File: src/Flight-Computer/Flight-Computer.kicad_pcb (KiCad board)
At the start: 4 copper layers, 101.6 x 50.8 mm, 60 parts, among them J1 Jumper_NO, P1 EJ508A, P2 USB, P3 SBH11-PBPC-D05-RA-BK, P4 0901471110, P5 66953-005LF, P6 Micro_SD_Card, P7 0901471110, U1 STM32H750VBTx, U2 LM22672MRE-5.0_NOPB, U3 LMS8117AMP-3.3_NOPB, U4 SN74LV07ADR, U5 SST25VF040B-50-4I-S2AE-T, U6 TPS2115APWR

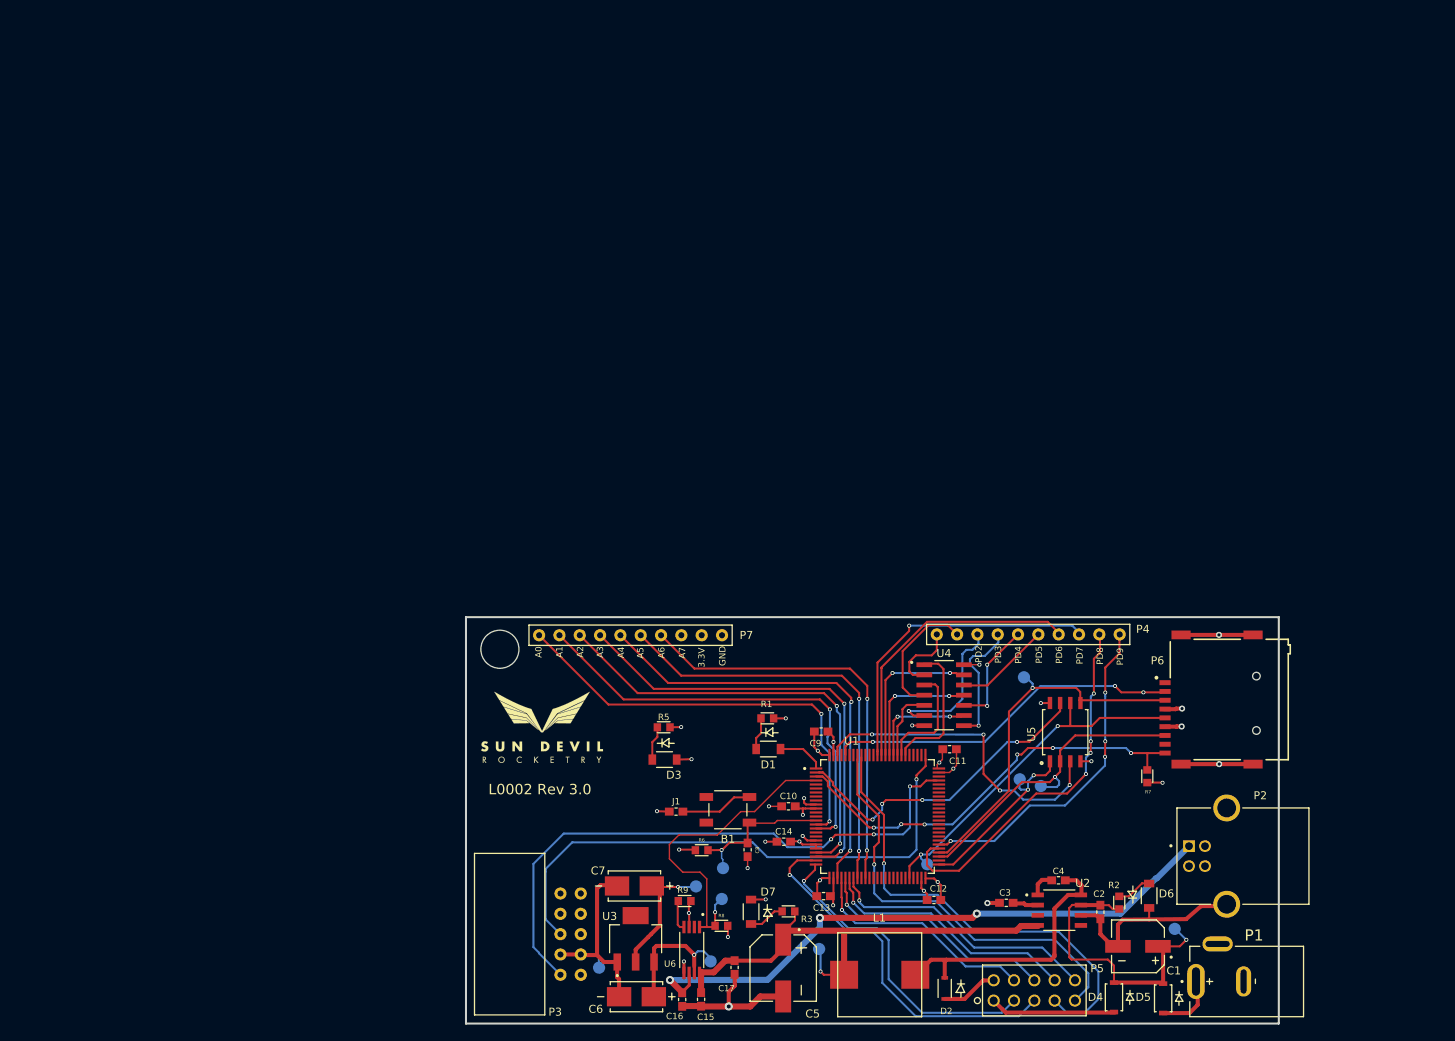
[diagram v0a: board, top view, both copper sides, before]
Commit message: setup layout design rules
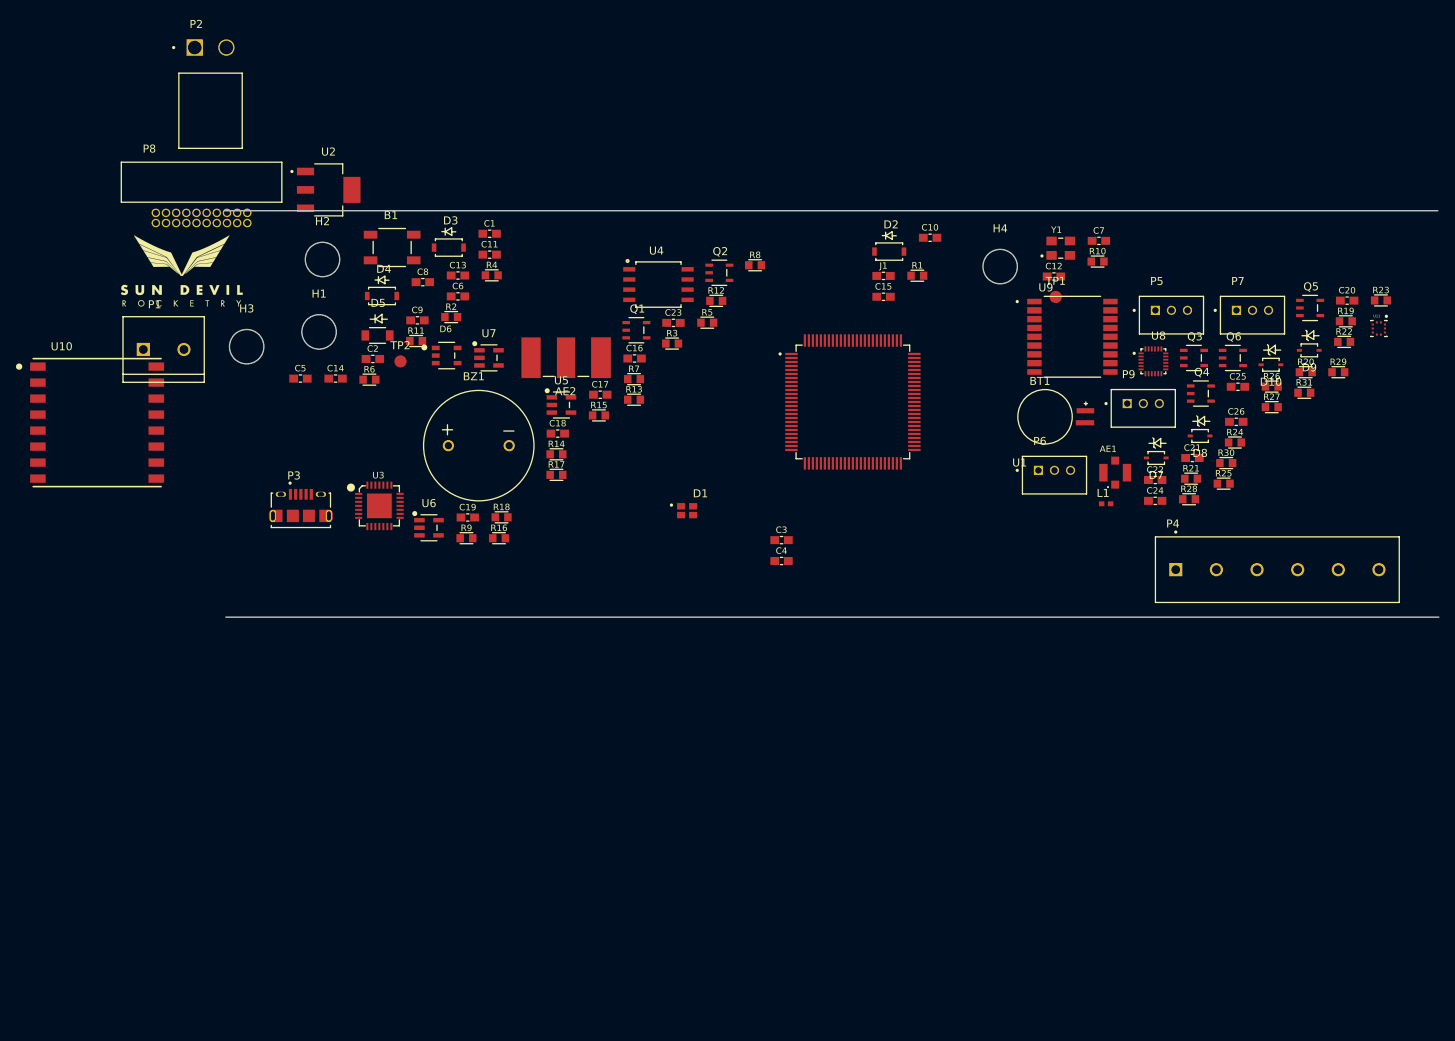
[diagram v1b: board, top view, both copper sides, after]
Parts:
- removed G***: LOGO, logo:Logo
- removed TP10, TP11, TP6, TP7, TP8, TP9: TP, Engine-Controller:TP
- removed TP3: TPGND, Engine-Controller:TP
- removed TP4: TP5V, Engine-Controller:TP
- removed TP5: 3.3V, Engine-Controller:TP
- added AE1: 0734120110, Flight-Computer:73412-0110, F.Cu at (182.9, 83.5)
- added AE2: 142-0701-851, Flight-Computer:142-0701-851, F.Cu at (114.1, 69.0)
- added BT1: MS614SE-FL28E, Flight-Computer:MS621FE-FL11E, F.Cu at (174.0, 76.6)
- added BZ1: AT-1438-TWT-R, Flight-Computer:AT-1438-TWT-R, F.Cu at (103.2, 80.2)
- added C18: 1uF, Flight-Computer:CAP_0603, F.Cu at (113.1, 78.7)
- added C19: 1uF, Flight-Computer:CAP_0603, F.Cu at (101.8, 89.1)
- added C20: 0.1uF, Flight-Computer:CAP_0603, F.Cu at (211.7, 62.0)
- added C21: 0.1uF, Flight-Computer:CAP_0603, F.Cu at (192.4, 81.7)
- added C22: 0.01uF, Flight-Computer:CAP_0603, F.Cu at (187.8, 84.5)
- added C23: 0.1uF, Flight-Computer:CAP_0603, F.Cu at (127.5, 64.8)
- added C24: 0.1uF, Flight-Computer:CAP_0603, F.Cu at (187.8, 87.1)
- added C25: 0.1uF, Flight-Computer:CAP_0603, F.Cu at (198.1, 72.8)
- added C26: 0.01uF, Flight-Computer:CAP_0603, F.Cu at (197.9, 77.2)
- added D10: MM3Z3V3B, Flight-Computer:MM3Z3V3B, F.Cu at (202.2, 70.1)
- added D8: MM3Z3V3B, Flight-Computer:MM3Z3V3B, F.Cu at (193.4, 79.0)
- added D9: MM3Z3V3B, Flight-Computer:MM3Z3V3B, F.Cu at (207.0, 68.3)
- added H1: Mounting-Hole, Flight-Computer:MountingHole_4.3mm_M4_DIN965, F.Cu at (83.2, 65.9)
- added H2: Mounting-Hole, Flight-Computer:MountingHole_4.3mm_M4_DIN965, F.Cu at (83.7, 56.9)
- added H3: Mounting-Hole, Flight-Computer:MountingHole_4.3mm_M4_DIN965, F.Cu at (74.2, 67.8)
- added H4: Mounting-Hole, Flight-Computer:MountingHole_4.3mm_M4_DIN965, F.Cu at (168.4, 57.8)
- added LOGO1: Logo, Flight-Computer:Logo, F.Cu at (66.1, 58.1)
- added P8: 3220-20-0200-00, Flight-Computer:3220-20-0200-00, F.Cu at (68.5, 51.1)
- added P9: 440054-3, Flight-Computer:440054-3, F.Cu at (184.3, 74.9)
- added Q1: QS5U17TR, Engine-Controller:QS5U17TR, F.Cu at (122.9, 65.7)
- added Q2: QS5U17TR, Engine-Controller:QS5U17TR, F.Cu at (133.3, 58.6)
- added Q3: QS5U17TR, Engine-Controller:QS5U17TR, F.Cu at (192.6, 69.2)
- added Q4: QS5U17TR, Engine-Controller:QS5U17TR, F.Cu at (193.5, 73.7)
- added Q5: QS5U17TR, Engine-Controller:QS5U17TR, F.Cu at (207.1, 63.0)
- added Q6: QS5U17TR, Engine-Controller:QS5U17TR, F.Cu at (197.5, 69.2)
- added R10: 100k, Flight-Computer:RES_0603, F.Cu at (180.6, 57.2)
- added R11: 100k, Flight-Computer:RES_0603, F.Cu at (95.4, 67.1)
- added R12: 100k, Flight-Computer:RES_0603, F.Cu at (132.9, 62.1)
- added R13: 100k, Flight-Computer:RES_0603, F.Cu at (122.6, 74.4)
- added R14: 10k, Flight-Computer:RES_0603, F.Cu at (112.9, 81.2)
- added R15: 1k, Flight-Computer:RES_0603, F.Cu at (118.2, 76.4)
- added R16: 10k, Flight-Computer:RES_0603, F.Cu at (105.7, 91.7)
- added R17: 10k, Flight-Computer:RES_0603, F.Cu at (112.9, 83.8)
- added R18: 10k, Flight-Computer:RES_0603, F.Cu at (106.1, 89.1)
- added R19: 10k, Flight-Computer:RES_0603, F.Cu at (211.6, 64.6)
- added R20: 10k, Flight-Computer:RES_0603, F.Cu at (206.6, 71.0)
- added R21: 33, Flight-Computer:RES_0603, F.Cu at (192.2, 84.3)
- added R22: 33, Flight-Computer:RES_0603, F.Cu at (211.4, 67.2)
- added R23: 33, Flight-Computer:RES_0603, F.Cu at (216.0, 62.0)
- added R24: 33, Flight-Computer:RES_0603, F.Cu at (197.7, 79.8)
- added R25: 33, Flight-Computer:RES_0603, F.Cu at (196.3, 84.9)
- added R26: 33, Flight-Computer:RES_0603, F.Cu at (202.3, 72.8)
- added R27: 33, Flight-Computer:RES_0603, F.Cu at (202.3, 75.4)
- added R28: 33, Flight-Computer:RES_0603, F.Cu at (192.0, 86.9)
- added R29: 4.7k, Flight-Computer:RES_0603, F.Cu at (210.6, 71.0)
- added R30: 4.7k, Flight-Computer:RES_0603, F.Cu at (196.6, 82.3)
- added R31: 10, Flight-Computer:RES_0603, F.Cu at (206.4, 73.6)
- added R4: 82, Flight-Computer:RES_0603, F.Cu at (104.8, 58.9)
- added U10: RFM95W-868S2, Flight-Computer:RFM95, F.Cu at (55.5, 77.3)
- added U11: BMP390, Flight-Computer:BMP390, F.Cu at (215.8, 65.5)
- added U7: TS391IYLT, Flight-Computer:TS391IYLT, F.Cu at (104.5, 69.2)
- added U8: MPU-9250, Flight-Computer:MPU-9250, F.Cu at (187.5, 69.6)
- added U9: MAX-8C-0-10, Flight-Computer:MAX-8C-0, F.Cu at (177.4, 66.6)
- added Y1: ECS-240-18-33-JGN-TR, Flight-Computer:ECS-240-18-33-JGN-TR, F.Cu at (175.9, 55.5)
- B1: value SW_PTS647SM38SMTR2LFS_CNK -> PTS647SM38SMTR2LFS; footprint Engine-Controller:PTS647SM38SMTR2LFS -> Flight-Computer:PTS647SM38SMTR2LFS
- C1: value 68uF -> 4.7uF; footprint Engine-Controller:EEEFPV680XAP -> Flight-Computer:CAP_0603
- C10, C9: value 0.1u -> 8pF; footprint Engine-Controller:CAP_0603 -> Flight-Computer:CAP_0603
- C11: value 0.1u -> 1uF; footprint Engine-Controller:CAP_0603 -> Flight-Computer:CAP_0603
- C12, C13: value 0.1u -> 2.2uF; footprint Engine-Controller:CAP_0603 -> Flight-Computer:CAP_0603
- C14: value 0.1u -> 10uF; footprint Engine-Controller:CAP_0603 -> Flight-Computer:CAP_0603
- C15: value 0.1uF -> 10uF; footprint Engine-Controller:CAP_0603 -> Flight-Computer:CAP_0603
- C16: value 0.1uF -> 1uF; footprint Engine-Controller:CAP_0603 -> Flight-Computer:CAP_0603
- C17: value 1uF -> 0.1uF; footprint Engine-Controller:CAP_0603 -> Flight-Computer:CAP_0603
- C2: value 2.2uF -> 0.1uF; footprint Engine-Controller:CAP_0603 -> Flight-Computer:CAP_0603
- C3: value 1 uF -> 0.1uF; footprint Engine-Controller:CAP_0603 -> Flight-Computer:CAP_0603
- C4: value 10 nF -> 0.1uF; footprint Engine-Controller:CAP_0603 -> Flight-Computer:CAP_0603
- C5: value 150uF -> 0.1uF; footprint Engine-Controller:CAP_EEEFP1E151AL -> Flight-Computer:CAP_0603
- C6, C7: value 10uF -> 0.1uF; footprint Engine-Controller:CWR11HH106KB -> Flight-Computer:CAP_0603
- C8: value 0.1u -> 0.1uF; footprint Engine-Controller:CAP_0603 -> Flight-Computer:CAP_0603
- D1: value 150120AS75000 -> CLMVC-FKA-CL1D1L71BB7C3C3; footprint Engine-Controller:150120AS75000 -> Flight-Computer:CLMVC-FKA-CL1D1L71BB7C3C3
- D2: value RB160VAM-60TR -> SM5819PL-TP; footprint Engine-Controller:RB160VAM-60TR -> Flight-Computer:SM5819PL-TP
- D3: value SML-LX1206GC-TR -> SM5819PL-TP; footprint Engine-Controller:SML-LX1206GC-TR -> Flight-Computer:SM5819PL-TP
- D4: footprint Engine-Controller:SM5819PL-TP -> Flight-Computer:SM5819PL-TP
- D5: value SM5819PL-TP -> SML-LX1206GC-TR; footprint Engine-Controller:SM5819PL-TP -> Flight-Computer:SML-LX1206GC-TR
- D6: value SML-LX1206GC-TR -> SP0504BAHTG; footprint Engine-Controller:SML-LX1206GC-TR -> Flight-Computer:SP0504BAHTG
- D7: value SML-LX1206GC-TR -> MM3Z3V3B; footprint Engine-Controller:SML-LX1206GC-TR -> Flight-Computer:MM3Z3V3B
- J1: footprint Engine-Controller:Jumper-NO -> Flight-Computer:Jumper-NO
- L1: value 33uH -> 27nH; footprint Engine-Controller:SRP1038A-330M -> Flight-Computer:L-07C27NJV6T
- P1: value EJ508A -> 282837-2; footprint Engine-Controller:12V_power_jack -> Flight-Computer:282837-2
- P2: value USB -> 647676-2; footprint Engine-Controller:USB-TypeB -> Flight-Computer:647676-2
- P3: value SBH11-PBPC-D05-RA-BK -> USB; footprint Engine-Controller:SBH11-PBPC-D05-RA-BK -> Flight-Computer:10118194-0001LF
- P4: value 0901471110 -> 282837-6; footprint Engine-Controller:0901471110 -> Flight-Computer:282837-6
- P5: value 66953-005LF -> 440054-3; footprint Engine-Controller:66953-005LF -> Flight-Computer:440054-3
- P6: value Micro_SD_Card -> 440054-3; footprint Engine-Controller:GCT_MEM2075-00-140-01-A -> Flight-Computer:440054-3
- P7: value 0901471110 -> 440054-3; footprint Engine-Controller:0901471110 -> Flight-Computer:440054-3
- R1: value 240 -> 68; footprint Engine-Controller:RES_0603 -> Flight-Computer:RES_0603
- R2: value 2k -> 240; footprint Engine-Controller:RES_0603 -> Flight-Computer:RES_0603
- R3: value 470 -> 4.7k; footprint Engine-Controller:RES_0603 -> Flight-Computer:RES_0603
- R5: value 240 -> 10k; footprint Engine-Controller:RES_0603 -> Flight-Computer:RES_0603
- R6: value 10k -> 280; footprint Engine-Controller:RES_0603 -> Flight-Computer:RES_0603
- R7, R8: footprint Engine-Controller:RES_0603 -> Flight-Computer:RES_0603
- R9: value 470 -> 10k; footprint Engine-Controller:RES_0603 -> Flight-Computer:RES_0603
- TP1: value TPNRST -> TP; footprint Engine-Controller:TP -> Flight-Computer:TP; moved to F.Cu
- TP2: value TPVIN -> TP; footprint Engine-Controller:TP -> Flight-Computer:TP; moved to F.Cu
- U1: footprint Engine-Controller:STM32H750VBT6 -> Flight-Computer:STM32H750VBT6
- U2: value LM22672MRE-5.0_NOPB -> LMS8117AMP-3.3_NOPB; footprint Engine-Controller:LM22672MRE-5.0_NOPB -> Flight-Computer:LMS8117AMP-3.3NOPB
- U3: value LMS8117AMP-3.3_NOPB -> CP2102-GMR(QFN28); footprint Engine-Controller:SOT-223 -> Flight-Computer:CP2012-GMR
- U4: value SN74LV07ADR -> SST25VF040B-50-4I-S2AE-T; footprint Engine-Controller:SN74LV07ADR -> Flight-Computer:SST25VF040B-50-4I-S2AE-T
- U5: value SST25VF040B-50-4I-S2AE-T -> TS391IYLT; footprint Engine-Controller:SST25VF040B-50-4I-S2AE-T -> Flight-Computer:TS391IYLT
- U6: value TPS2115APWR -> TS391IYLT; footprint Engine-Controller:TPS2115APWR -> Flight-Computer:TS391IYLT
- moved P2 161.8 mm to (67.7, 30.4), turned to 0 degrees
- moved P1 153.6 mm to (63.8, 68.1), turned to 0 degrees
- moved D5 128.5 mm to (90.5, 66.4), turned to 0 degrees
- moved U2 128.2 mm to (84.4, 48.2)
- moved D4 126.7 mm to (91.1, 61.5), turned to 0 degrees
- moved C1 120.4 mm to (104.6, 53.7), turned to 0 degrees
- moved TP2 120.0 mm to (93.4, 69.6)
- moved C2 114.2 mm to (90.0, 69.3), turned to 0 degrees
- moved R2 111.0 mm to (99.8, 64.1), turned to 0 degrees
- moved D6 110.8 mm to (99.2, 68.9), turned to 0 degrees
- moved C7 99.4 mm to (180.7, 54.6), turned to 0 degrees
- moved C5 95.2 mm to (80.9, 71.8), turned to 0 degrees
- moved D2 92.4 mm to (154.5, 55.9), turned to 0 degrees
- moved C15 90.7 mm to (153.8, 61.6), turned to 0 degrees
- moved C6 90.3 mm to (100.6, 61.5), turned to 0 degrees
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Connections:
- B1 pad 1: /NRST -> Earth
- B1 pad 2: Net-(B1-Pad2) -> unconnected-(B1-Pad2)
- B1 pad 3: Net-(B1-Pad3) -> NRST
- B1 pad 4: Net-(B1-Pad4) -> unconnected-(B1-Pad4)
- C1 pad 1: /power/VIN -> 3.3V
- C10 pad 1: Earth -> OSC_OUT
- C10 pad 2: 3.3V -> Earth
- C11 pad 1: Earth -> 3.3V
- C11 pad 2: 3.3V -> Earth
- C12 pad 1: Earth -> CAP1
- C12 pad 2: 3.3V -> Earth
- C13 pad 1: Earth -> CAP2
- C13 pad 2: 3.3V -> Earth
- C14 pad 1: Earth -> VIN
- C14 pad 2: 3.3V -> Earth
- C15 pad 1: Earth -> 3.3V
- C15 pad 2: 5V_BUCK -> Earth
- C16 pad 1: Earth -> 5V
- C16 pad 2: 5V_USB -> Earth
- C17 pad 1: Earth -> 5V
- C17 pad 2: 5V_BUCK -> Earth
- C2 pad 1: Earth -> 3.3V
- C2 pad 2: /power/VIN -> Earth
- C3 pad 1: Earth -> 3.3V
- C3 pad 2: Net-(C3-Pad2) -> Earth
- C4 pad 1: Net-(C4-Pad1) -> 3.3V
- C4 pad 2: Net-(C4-Pad2) -> Earth
- C5 pad 1: 5V_BUCK -> 3.3V
- C6 pad 1: /power/5V -> 3.3V
- C8 pad 1: Earth -> NRST
- C8 pad 2: /NRST -> Earth
- C9 pad 1: Earth -> OSC_IN
- C9 pad 2: 3.3V -> Earth
- D1 pad 1: Net-(D1-Pad1) -> 3.3V
- D1 pad 2: /MCU_STATUS -> Net-(D1-Pad2)
- D2 pad 1: Net-(C4-Pad1) -> VIN
- D2 pad 2: Earth -> 5V
- D3 pad 1: Net-(D3-Pad1) -> VIN
- D3 pad 2: 3.3V -> /PIN_SCREW
- D4 pad 1: /power/VIN -> VIN
- D4 pad 2: V_HEAD -> /PIN_HARN
- D5 pad 1: /power/VIN -> Net-(D5-Pad1)
- D5 pad 2: /power/V_JACK -> 3.3V
- D6 pad 1: Earth -> 5V
- D6 pad 2: Net-(D6-Pad2) -> Earth
- D7 pad 1: Earth -> MOTOR1_PWM
- D7 pad 2: Net-(D7-Pad2) -> Earth
- J1 pad 1: Earth -> 3.3V
- J1 pad 2: Net-(B1-Pad3) -> BOOT
- L1 pad 1: Net-(C4-Pad1) -> /Navigation and Control/GPS
- L1 pad 2: 5V_BUCK -> Net-(C26-Pad1)
- P1 pad 1: /power/V_JACK -> Earth
- P1 pad 2: Earth -> /PIN_SCREW
- P2 pad 1: 5V_USB -> /PIN_HARN
- P2 pad 2: Net-(P2-Pad2) -> Earth
- P4 pad 1: /Connectors/PD0_BUF -> VIN
- P4 pad 2: /Connectors/PD1_BUF -> VIN_SW
- P4 pad 3: /Connectors/PD2_BUF -> VIN_SW
- P4 pad 4: /Connectors/PD3_BUF -> Net-(P4-Pad4)
- P4 pad 5: /Connectors/PD4_BUF -> VIN_SW
- P4 pad 6: /Connectors/PD5_BUF -> Net-(P4-Pad6)
- P7 pad 1: A0 -> VIN
- P7 pad 2: A1 -> MOTOR2_PWM
- P7 pad 3: A2 -> Net-(P7-Pad3)
- R1 pad 1: Net-(D1-Pad1) -> STATUS_B
- R1 pad 2: Earth -> Net-(D1-Pad2)
- R2 pad 1: /power/VIN -> Earth
- R2 pad 2: Net-(D6-Pad2) -> Net-(D5-Pad1)
- R3 pad 1: 5V_BUCK -> 3.3V
- R3 pad 2: Net-(D7-Pad2) -> ~{USB_RST}
- R5 pad 1: Net-(D3-Pad1) -> Earth
- R5 pad 2: Earth -> ~{USB_SUSPEND}
- R6 pad 1: 3.3V -> STATUS_R
- R6 pad 2: /NRST -> Net-(D1-Pad4)
- R7 pad 1: SD_DETECT -> ~{FLASH_SS}
- R8 pad 1: 5V_SRC -> Earth
- R8 pad 2: 3.3V -> FLASH_MOSI
- R9 pad 1: Net-(R9-Pad1) -> Earth
- R9 pad 2: Earth -> VIN_SW
- TP1 pad 1: /NRST -> NRST
- TP2 pad 1: /power/VIN -> 3.3V
- U1 pad 1: /MCU_STATUS -> W_SCK
- U1 pad 12: Net-(U1-Pad12) -> OSC_IN
- U1 pad 13: Net-(U1-Pad13) -> OSC_OUT
- U1 pad 14: /NRST -> NRST
- U1 pad 15: A0 -> W_SS
- U1 pad 16: A1 -> W_RST
- U1 pad 17: Net-(U1-Pad17) -> W_IO0
- U1 pad 18: Net-(U1-Pad18) -> W_IO1
- U1 pad 2: FLASH_HOLD -> unconnected-(U1-Pad2)
- U1 pad 22: A2 -> GPS_RX
- U1 pad 23: A3 -> GPS_TX
- U1 pad 24: TX -> MOTOR1_PWM
- U1 pad 25: RX -> MOTOR2_PWM
- U1 pad 28: A4 -> MOTOR1_EN
- U1 pad 29: SCK -> MOTOR3_PWM
- U1 pad 3: SD_DETECT -> unconnected-(U1-Pad3)
- U1 pad 30: MISO -> MOTOR4_PWM
- U1 pad 31: MOSI -> BEEP
- U1 pad 32: SS -> W_IO2
- U1 pad 33: A5 -> W_IO3
- U1 pad 34: Net-(U1-Pad34) -> unconnected-(U1-Pad34)
- U1 pad 35: A6 -> unconnected-(U1-Pad35)
- U1 pad 36: Net-(U1-Pad36) -> unconnected-(U1-Pad36)
- U1 pad 37: Net-(U1-Pad37) -> unconnected-(U1-Pad37)
- U1 pad 38: Net-(U1-Pad38) -> unconnected-(U1-Pad38)
- U1 pad 39: Net-(U1-Pad39) -> unconnected-(U1-Pad39)
- U1 pad 4: 5V_SRC -> W_MISO
- U1 pad 40: Net-(U1-Pad40) -> STATUS_R
- U1 pad 41: Net-(U1-Pad41) -> STATUS_G
- U1 pad 42: Net-(U1-Pad42) -> STATUS_B
- U1 pad 43: Net-(U1-Pad43) -> unconnected-(U1-Pad43)
- U1 pad 44: Net-(U1-Pad44) -> unconnected-(U1-Pad44)
- U1 pad 45: Net-(U1-Pad45) -> unconnected-(U1-Pad45)
- U1 pad 46: FLASH_SCK -> BP_SCL
- U1 pad 47: Net-(U1-Pad47) -> BP_SDA
- U1 pad 48: Net-(U1-Pad48) -> CAP1
- U1 pad 5: Net-(U1-Pad5) -> W_MOSI
- U1 pad 51: FLASH_SS -> ~{FLASH_SS}
- U1 pad 52: Net-(U1-Pad52) -> FLASH_SCK
- U1 pad 55: PD8 -> ~{MAIN_CONT}
- U1 pad 56: PD9 -> ~{DROGUE_CONT}
- U1 pad 57: Net-(U1-Pad57) -> ~{USB_RST}
- U1 pad 58: Net-(U1-Pad58) -> ~{USB_SUSPEND}
- U1 pad 59: Net-(U1-Pad59) -> ~{FLASH_WP}
- U1 pad 6: Net-(U1-Pad6) -> unconnected-(U1-Pad6)
- U1 pad 60: Net-(U1-Pad60) -> ~{FLASH_HOLD}
- U1 pad 61: Net-(U1-Pad61) -> unconnected-(U1-Pad61)
- U1 pad 62: Net-(U1-Pad62) -> unconnected-(U1-Pad62)
- U1 pad 63: Net-(U1-Pad63) -> W_IO4
- U1 pad 64: Net-(U1-Pad64) -> W_IO5
- U1 pad 65: Net-(U1-Pad65) -> unconnected-(U1-Pad65)
- U1 pad 66: Net-(U1-Pad66) -> unconnected-(U1-Pad66)
- U1 pad 67: Net-(U1-Pad67) -> MOTOR3_EN
- U1 pad 68: Net-(U1-Pad68) -> RX_USB
- U1 pad 69: Net-(U1-Pad69) -> TX_USB
- U1 pad 7: Net-(U1-Pad7) -> unconnected-(U1-Pad7)
- U1 pad 70: Net-(U1-Pad70) -> MOTOR2_EN
- U1 pad 71: Net-(U1-Pad71) -> MOTOR4_EN
- U1 pad 73: Net-(U1-Pad73) -> CAP2
- U1 pad 77: Net-(U1-Pad77) -> ~{GPS_RST}
- U1 pad 78: Net-(U1-Pad78) -> unconnected-(U1-Pad78)
- U1 pad 79: Net-(U1-Pad79) -> unconnected-(U1-Pad79)
- U1 pad 8: Net-(U1-Pad8) -> unconnected-(U1-Pad8)
- U1 pad 80: Net-(U1-Pad80) -> unconnected-(U1-Pad80)
- U1 pad 81: PD0 -> ~{GPS_SBOOT}
- U1 pad 82: PD1 -> GPS_INT
- U1 pad 83: PD2 -> BP_INT
- U1 pad 84: PD3 -> IMU_INT
- U1 pad 85: PD4 -> GPS_TIM
- U1 pad 86: PD5 -> DROGUE
- U1 pad 87: PD6 -> ~{SWITCH}
- U1 pad 88: PD7 -> MAIN
- U1 pad 89: Net-(U1-Pad89) -> SWO
- U1 pad 9: Net-(U1-Pad9) -> unconnected-(U1-Pad9)
- U1 pad 90: Net-(U1-Pad90) -> unconnected-(U1-Pad90)
- U1 pad 91: Net-(U1-Pad91) -> unconnected-(U1-Pad91)
- U1 pad 94: Net-(U1-Pad94) -> BOOT
- U1 pad 95: Net-(U1-Pad95) -> unconnected-(U1-Pad95)
- U1 pad 96: SD_SS -> unconnected-(U1-Pad96)
- U1 pad 97: Net-(U1-Pad97) -> unconnected-(U1-Pad97)
- U1 pad 98: FLASH_WP -> unconnected-(U1-Pad98)
- U2 pad 1: Net-(C4-Pad2) -> Earth
- U2 pad 2: Net-(C3-Pad2) -> 3.3V
- U2 pad 3: Net-(U2-Pad3) -> VIN
- U3 pad 1: Earth -> unconnected-(U3-Pad1)
- U3 pad 2: 3.3V -> unconnected-(U3-Pad2)
- U3 pad 3: /power/5V -> Earth
- U3 pad 4: (no net) -> /Peripherals/D+
- U4 pad 1: PD0 -> ~{FLASH_SS}
- U4 pad 2: /Connectors/PD0_BUF -> FLASH_MISO
- U4 pad 3: PD1 -> ~{FLASH_WP}
- U4 pad 4: /Connectors/PD1_BUF -> Earth
- U4 pad 5: PD2 -> FLASH_MOSI
- U4 pad 6: /Connectors/PD2_BUF -> FLASH_SCK
- U4 pad 7: Earth -> ~{FLASH_HOLD}
- U4 pad 8: /Connectors/PD3_BUF -> 3.3V
- U5 pad 1: FLASH_SS -> ~{SWITCH}
- U5 pad 2: FLASH_MISO -> Earth
- U5 pad 3: FLASH_WP -> VCOMP
- U5 pad 4: Earth -> VIN_SW
- U5 pad 5: FLASH_MOSI -> VIN
- U6 pad 1: 5V_SRC -> ~{MAIN_CONT}
- U6 pad 2: Net-(U6-Pad2) -> Earth
- U6 pad 3: Earth -> VCOMP
- U6 pad 4: Net-(R9-Pad1) -> Net-(P4-Pad6)
- U6 pad 5: Earth -> VIN
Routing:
- net Earth: track 135.0 -> 0.00 mm, vias 22 -> 0
- net 5V_USB: track 77.2 -> 0.00 mm, vias 3 -> 0
- net SWDIO: track 74.4 -> 0.00 mm, vias 3 -> 0
- net SWCLK: track 69.8 -> 0.00 mm, vias 1 -> 0
- net 5V_BUCK: track 64.5 -> 0.00 mm, vias 1 -> 0
- net SCL: track 58.9 -> 0.00 mm, vias 1 -> 0
- net A2: track 56.6 -> 0.00 mm, vias 2 -> 0
- net A3: track 56.2 -> 0.00 mm, vias 2 -> 0
- net A4: track 55.4 -> 0.00 mm, vias 2 -> 0
- net A1: track 55.4 -> 0.00 mm, vias 2 -> 0
- net A0: track 55.1 -> 0.00 mm, vias 2 -> 0
- net SD_DETECT: track 53.6 -> 0.00 mm, vias 6 -> 0
- net A5: track 53.5 -> 0.00 mm, vias 2 -> 0
- net SDA: track 53.1 -> 0.00 mm, vias 1 -> 0
- net A6: track 52.5 -> 0.00 mm, vias 2 -> 0
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- removed copper zone on In2.Cu, net 3.3V
- removed copper zone on In1.Cu, net Earth
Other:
- board size 101.6 x 50.8 mm -> 151.8 x 50.8 mm
- net class Default removed
- net class Micro removed
- net class Power removed
- board text removed: "3.3V"
- board text removed: "A0"
- board text removed: "A1"
- board text removed: "A2"
- board text removed: "A3"
- board text removed: "A4"
- board text removed: "A5"
- board text removed: "A6"
- board text removed: "A7"
- board text removed: "GND"
- board text removed: "L0002 Rev 3.0"
- board text removed: "MISO"
- board text removed: "MOSI"
- board text removed: "PD0"
- board text removed: "PD1"
- board text removed: "PD2"
- board text removed: "PD3"
- board text removed: "PD4"
- board text removed: "PD5"
- board text removed: "PD6"
- board text removed: "PD7"
- board text removed: "PD8"
- board text removed: "PD9"
- board text removed: "RX"
- board text removed: "SCK"
- board text removed: "SCL"
- board text removed: "SDA"
- board text removed: "SS"
- board text removed: "TX"
- board text removed: "VIN"

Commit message: placed pcb parts on board and defined form factor
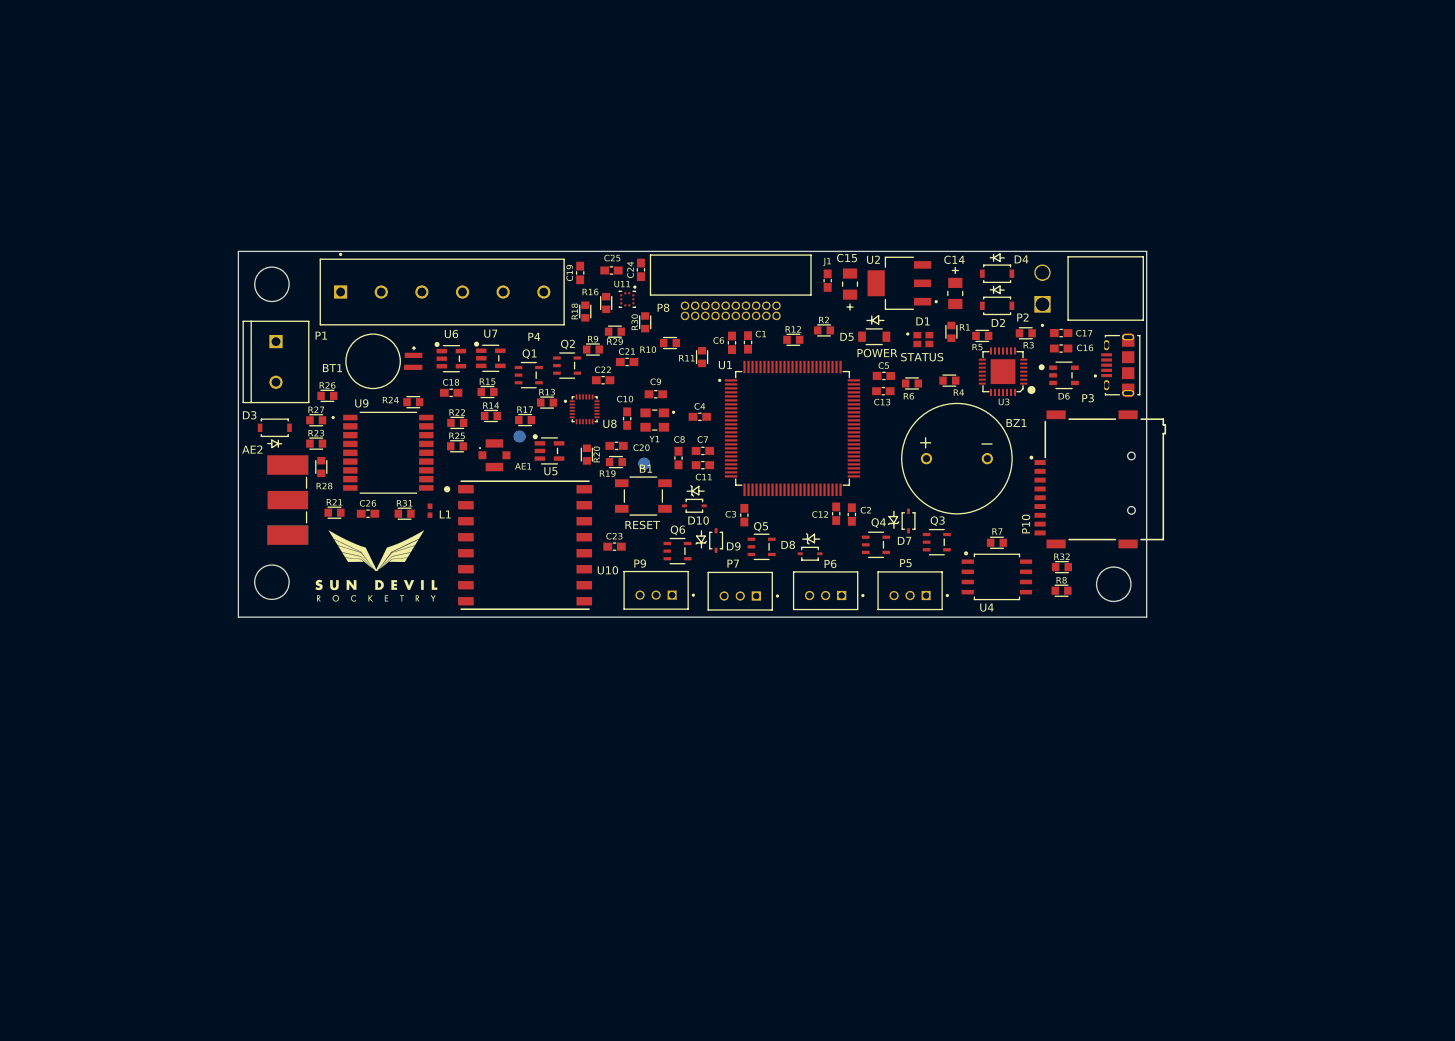
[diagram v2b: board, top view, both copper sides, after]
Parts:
- removed H2: Mounting-Hole, Flight-Computer:MountingHole_4.3mm_M4_DIN965
- added P10: Micro_SD_Card, Flight-Computer:MEM2075-00-140-01-A, F.Cu at (184.8, 84.9)
- added R32: 10k, Flight-Computer:RES_0603, F.Cu at (176.1, 95.4)
- AE2: value 142-0701-851 -> CONN_142-0701-851_CIN
- C14, C15: footprint Flight-Computer:CAP_0603 -> Flight-Computer:T491A106K010AT
- TP1, TP2: moved to B.Cu
- moved R23 134.3 mm to (82.9, 79.9)
- moved R27 119.5 mm to (82.9, 77.0)
- moved R26 118.1 mm to (84.3, 73.9)
- moved R31 113.5 mm to (93.9, 88.7)
- moved R22 111.3 mm to (100.5, 77.3)
- moved P2 110.7 mm to (173.7, 62.5), turned to 90 degrees
- moved P4 110.0 mm to (98.6, 61.0)
- moved C26 109.1 mm to (89.4, 88.7)
- moved R28 108.5 mm to (83.5, 82.8), turned to -90 degrees
- moved R21 107.2 mm to (85.2, 88.5)
- moved P3 105.1 mm to (184.4, 70.1), turned to 90 degrees
- moved R24 102.8 mm to (95.0, 74.7)
- moved R25 95.9 mm to (100.5, 80.2)
- moved U11 94.0 mm to (121.8, 61.9)
- moved C20 93.1 mm to (120.4, 80.2)
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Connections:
- D6 pad 1: 5V -> /Peripherals/D+
- D6 pad 4: /Peripherals/D+ -> 5V
- R8 pad 2: FLASH_MOSI -> FLASH_SCK
- U1 pad 61: unconnected-(U1-Pad61) -> BP_INT
- U1 pad 65: unconnected-(U1-Pad65) -> SD_DAT0
- U1 pad 66: unconnected-(U1-Pad66) -> SD_DAT1
- U1 pad 78: unconnected-(U1-Pad78) -> SD_DAT2
- U1 pad 79: unconnected-(U1-Pad79) -> SD_DAT3
- U1 pad 80: unconnected-(U1-Pad80) -> SD_CLK
- U1 pad 83: BP_INT -> SD_CMD
- U1 pad 96: unconnected-(U1-Pad96) -> ~{SD_DETECT}
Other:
- board size 151.8 x 50.8 mm -> 113.5 x 45.7 mm
- board text added: "A0002 Flight Computer Rev 1.0"
- board text added: "POWER"
- board text added: "RESET"
- board text added: "STATUS"
